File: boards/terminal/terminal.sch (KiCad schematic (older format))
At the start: 108 parts, among them J1 Conn_01x14, J2 Conn_01x14, SW1 SW_Push_45deg, SW10 SW_Push_45deg, SW11 SW_Push_45deg, SW12 SW_Push_45deg, SW13 SW_Push_45deg, SW14 SW_Push_45deg, SW15 SW_Push_45deg, SW16 SW_Push_45deg, SW17 SW_Push_45deg, SW18 SW_Push_45deg, SW19 SW_Push_45deg, SW2 SW_Push_45deg, SW20 SW_Push_45deg, SW21 SW_Push_45deg, SW22 SW_Push_45deg, SW23 SW_Push_45deg, SW24 SW_Push_45deg, SW25 SW_Push_45deg, SW26 SW_Push_45deg, SW27 SW_Push_45deg, SW28 SW_Push_45deg, SW29 SW_Push_45deg, SW3 SW_Push_45deg, SW30 SW_Push_45deg, SW31 SW_Push_45deg, SW32 SW_Push_45deg, SW33 SW_Push_45deg, SW34 SW_Push_45deg, SW35 SW_Push_45deg, SW36 SW_Push_45deg, SW37 SW_Push_45deg, SW38 SW_Push_45deg, SW39 SW_Push_45deg, SW4 SW_Push_45deg, SW40 SW_Push_45deg, SW41 SW_Push_45deg, SW42 SW_Push_45deg, SW43 SW_Push_45deg, SW44 SW_Push_45deg, SW45 SW_Push_45deg, SW46 SW_Push_45deg, SW47 SW_Push_45deg, SW48 SW_Push_45deg, SW49 SW_Push_45deg, SW5 SW_Push_45deg, SW50 SW_Push_45deg, SW51 SW_Push_45deg, SW52 SW_Push_45deg, SW53 SW_Push_45deg, SW54 SW_Push_45deg, SW55 SW_Push_45deg, SW56 SW_Push_45deg, SW57 SW_Push_45deg, SW58 SW_Push_45deg, SW59 SW_Push_45deg, SW6 SW_Push_45deg, SW60 SW_Push_45deg, SW61 SW_Push_45deg, SW62 SW_Push_45deg, SW63 SW_Push_45deg, SW64 SW_Push_45deg, SW65 SW_Push_45deg, SW66 SW_Push_45deg, SW67 SW_Push_45deg, SW68 SW_Push_45deg, SW69 SW_Push_45deg, SW7 SW_Push_45deg, SW70 SW_Push_45deg, SW71 SW_Push_45deg, SW72 SW_Push_45deg, SW73 SW_Push_45deg, SW74 SW_Push_45deg, SW76 SW_Push_45deg, SW77 SW_Push_45deg, SW78 SW_Push_45deg, SW79 SW_Push_45deg, SW8 SW_Push_45deg, SW80 SW_Push_45deg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

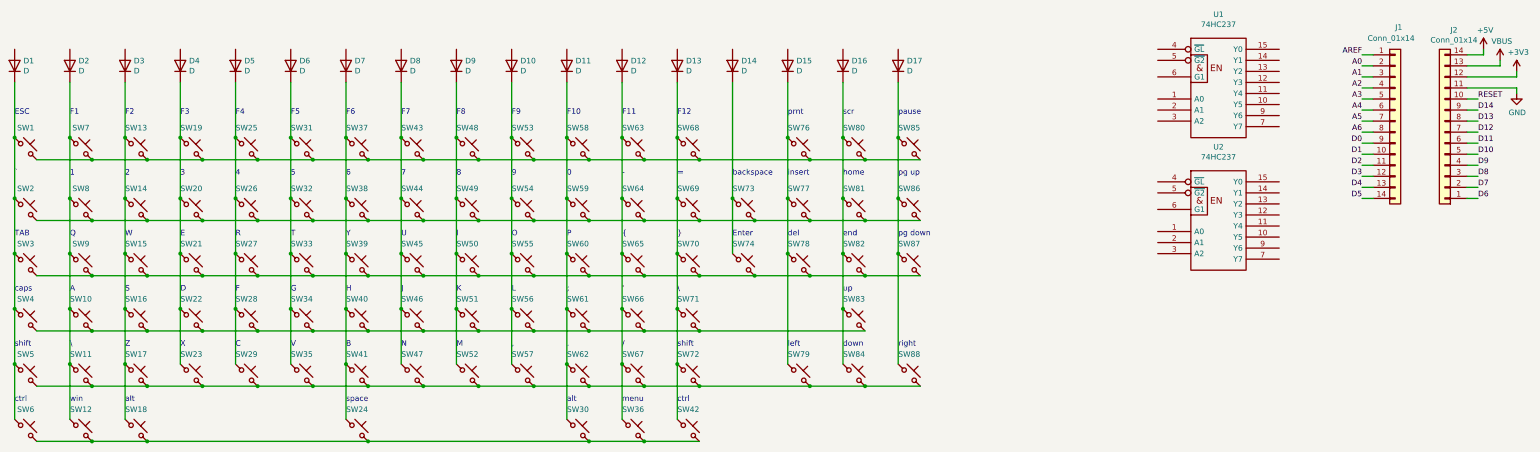
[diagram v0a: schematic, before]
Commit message: Fix keyboard layout
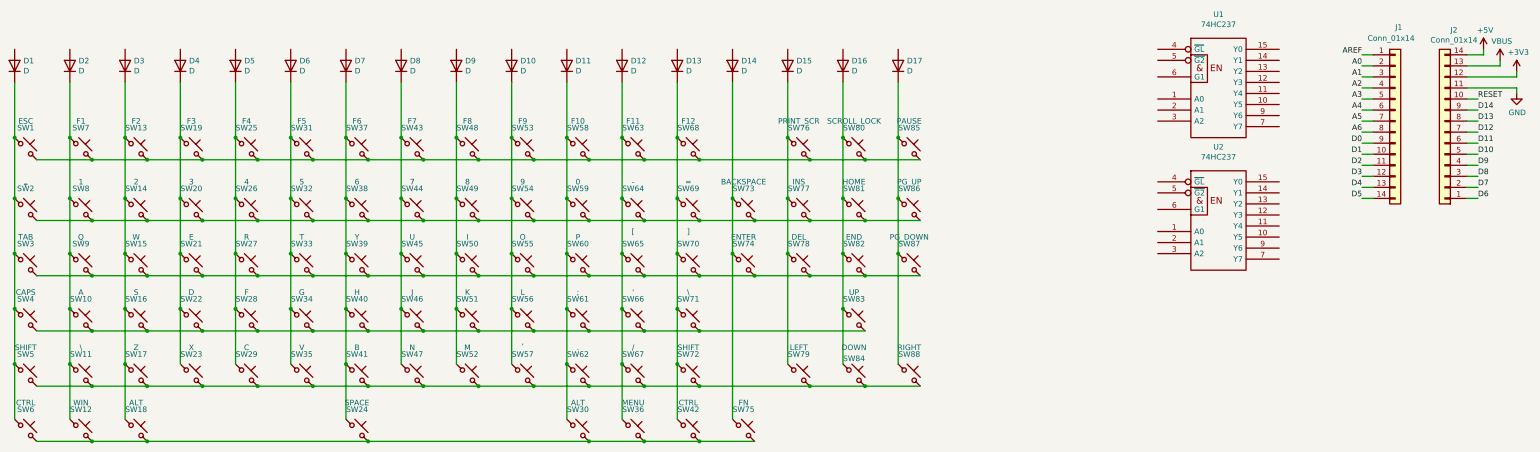
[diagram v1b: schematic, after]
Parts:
- added SW75: FN, Button_Switch_Keyboard:SW_Cherry_MX_1.00u_PCB, symbol Switch:SW_Push_45deg
- SW1: value SW_Push_45deg -> ESC
- SW10: value SW_Push_45deg -> A
- SW11, SW71: value SW_Push_45deg -> \\
- SW12: value SW_Push_45deg -> WIN
- SW13: value SW_Push_45deg -> F2
- SW14: value SW_Push_45deg -> 2
- SW15: value SW_Push_45deg -> W
- SW16: value SW_Push_45deg -> S
- SW17: value SW_Push_45deg -> Z
- SW18, SW30: value SW_Push_45deg -> ALT
- SW19: value SW_Push_45deg -> F3
- SW2: value SW_Push_45deg -> ~`
- SW20: value SW_Push_45deg -> 3
- SW21: value SW_Push_45deg -> E
- SW22: value SW_Push_45deg -> D
- SW23: value SW_Push_45deg -> X
- SW24: value SW_Push_45deg -> SPACE
- SW25: value SW_Push_45deg -> F4
- SW26: value SW_Push_45deg -> 4
- SW27: value SW_Push_45deg -> R
- SW28: value SW_Push_45deg -> F
- SW29: value SW_Push_45deg -> C
- SW3: value SW_Push_45deg -> TAB
- SW31: value SW_Push_45deg -> F5
- SW32: value SW_Push_45deg -> 5
- SW33: value SW_Push_45deg -> T
- SW34: value SW_Push_45deg -> G
- SW35: value SW_Push_45deg -> V
- SW36: value SW_Push_45deg -> MENU
- SW37: value SW_Push_45deg -> F6
- SW38: value SW_Push_45deg -> 6
- SW39: value SW_Push_45deg -> Y
- SW4: value SW_Push_45deg -> CAPS
- SW40: value SW_Push_45deg -> H
- SW41: value SW_Push_45deg -> B
- SW42: value SW_Push_45deg -> CTRL; footprint Button_Switch_Keyboard:SW_Cherry_MX_1.50u_PCB -> Button_Switch_Keyboard:SW_Cherry_MX_1.00u_PCB
- SW43: value SW_Push_45deg -> F7
- SW44: value SW_Push_45deg -> 7
- SW45: value SW_Push_45deg -> U
- SW46: value SW_Push_45deg -> J
- SW47: value SW_Push_45deg -> N
- SW48: value SW_Push_45deg -> F8
- SW49: value SW_Push_45deg -> 8
- SW5, SW72: value SW_Push_45deg -> SHIFT
- SW50: value SW_Push_45deg -> I
- SW51: value SW_Push_45deg -> K
- SW52: value SW_Push_45deg -> M
- SW53: value SW_Push_45deg -> F9
- SW54: value SW_Push_45deg -> 9
- SW55: value SW_Push_45deg -> O
- SW56: value SW_Push_45deg -> L
- SW57: value SW_Push_45deg -> ,
- SW58: value SW_Push_45deg -> F10
- SW59: value SW_Push_45deg -> 0
- SW6: value SW_Push_45deg -> CTRL
- SW60: value SW_Push_45deg -> P
- SW61: value SW_Push_45deg -> ;
- SW62: value SW_Push_45deg -> .
- SW63: value SW_Push_45deg -> F11
- SW64: value SW_Push_45deg -> -
- SW65: value SW_Push_45deg -> [
- SW66: value SW_Push_45deg -> '
- SW67: value SW_Push_45deg -> /
- SW68: value SW_Push_45deg -> F12
- SW69: value SW_Push_45deg -> =
- SW7: value SW_Push_45deg -> F1
- SW70: value SW_Push_45deg -> ]
- SW73: value SW_Push_45deg -> BACKSPACE
- SW74: value SW_Push_45deg -> ENTER
- SW76: value SW_Push_45deg -> PRINT_SCR
- SW77: value SW_Push_45deg -> INS
- SW78: value SW_Push_45deg -> DEL
- SW79: value SW_Push_45deg -> LEFT
- SW8: value SW_Push_45deg -> 1
- SW80: value SW_Push_45deg -> SCROLL_LOCK
- SW81: value SW_Push_45deg -> HOME
- SW82: value SW_Push_45deg -> END
- SW83: value SW_Push_45deg -> UP
- SW84: value SW_Push_45deg -> DOWN
- SW85: value SW_Push_45deg -> PAUSE
- SW86: value SW_Push_45deg -> PG_UP
- SW87: value SW_Push_45deg -> PG_DOWN
- SW88: value SW_Push_45deg -> RIGHT
- SW9: value SW_Push_45deg -> Q
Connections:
- net at D14.1 (K), SW73.1, SW74.1: now also SW75.1
- net at SW12.2, SW18.2, SW24.2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: now also SW75.2
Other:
- note removed: "'"
- note removed: ","
- note removed: "-"
- note removed: "."
- note removed: "/"
- note removed: "0"
- note removed: "1"
- note removed: "2"
- note removed: "3"
- note removed: "4"
- note removed: "5"
- note removed: "6"
- note removed: "7"
- note removed: "8"
- note removed: "9"
- note removed: ";"
- note removed: "="
- note removed: "A"
- note removed: "B"
- note removed: "C"
- note removed: "D"
- note removed: "E"
- note removed: "ESC"
- note removed: "Enter"
- note removed: "F"
- note removed: "F1"
- note removed: "F10"
- note removed: "F11"
- note removed: "F12"
- note removed: "F2"
- note removed: "F3"
- note removed: "F4"
- note removed: "F5"
- note removed: "F6"
- note removed: "F7"
- note removed: "F8"
- note removed: "F9"
- note removed: "G"
- note removed: "H"
- note removed: "I"
- note removed: "J"
- note removed: "K"
- note removed: "L"
- note removed: "M"
- note removed: "N"
- note removed: "O"
- note removed: "P"
- note removed: "Q"
- note removed: "R"
- note removed: "S"
- note removed: "T"
- note removed: "TAB"
- note removed: "U"
- note removed: "V"
- note removed: "W"
- note removed: "X"
- note removed: "Y"
- note removed: "Z"
- note removed: "\"
- note removed: "`"
- note removed: "alt"
- note removed: "backspace"
- note removed: "caps"
- note removed: "ctrl"
- note removed: "del"
- note removed: "down"
- note removed: "end"
- note removed: "home"
- note removed: "insert"
- note removed: "left"
- note removed: "menu"
- note removed: "pause"
- note removed: "pg down"
- note removed: "pg up"
- note removed: "prnt"
- note removed: "right"
- note removed: "scr"
- note removed: "shift"
- note removed: "space"
- note removed: "up"
- note removed: "win"
- note removed: "{"
- note removed: "}"
